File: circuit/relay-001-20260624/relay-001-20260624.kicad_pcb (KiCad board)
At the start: 2 copper layers, 169 x 126.3 mm, 15 parts, among them J1 Conn_01x03_Pin, J10 Conn_01x02_Pin, J11 Conn_01x02_Pin, J12 Conn_01x02_Pin, J13 Conn_01x02_Pin, J14 Conn_01x02_Pin, J15 Conn_01x02_Pin, J2 Conn_02x05_Odd_Even, J3 Conn_02x08_Odd_Even, J4 Conn_02x09_Odd_Even, J5 Conn_01x02_Pin, J6 Conn_01x02_Pin, J7 Conn_01x02_Pin, J8 Conn_01x02_Pin, J9 Conn_01x02_Pin

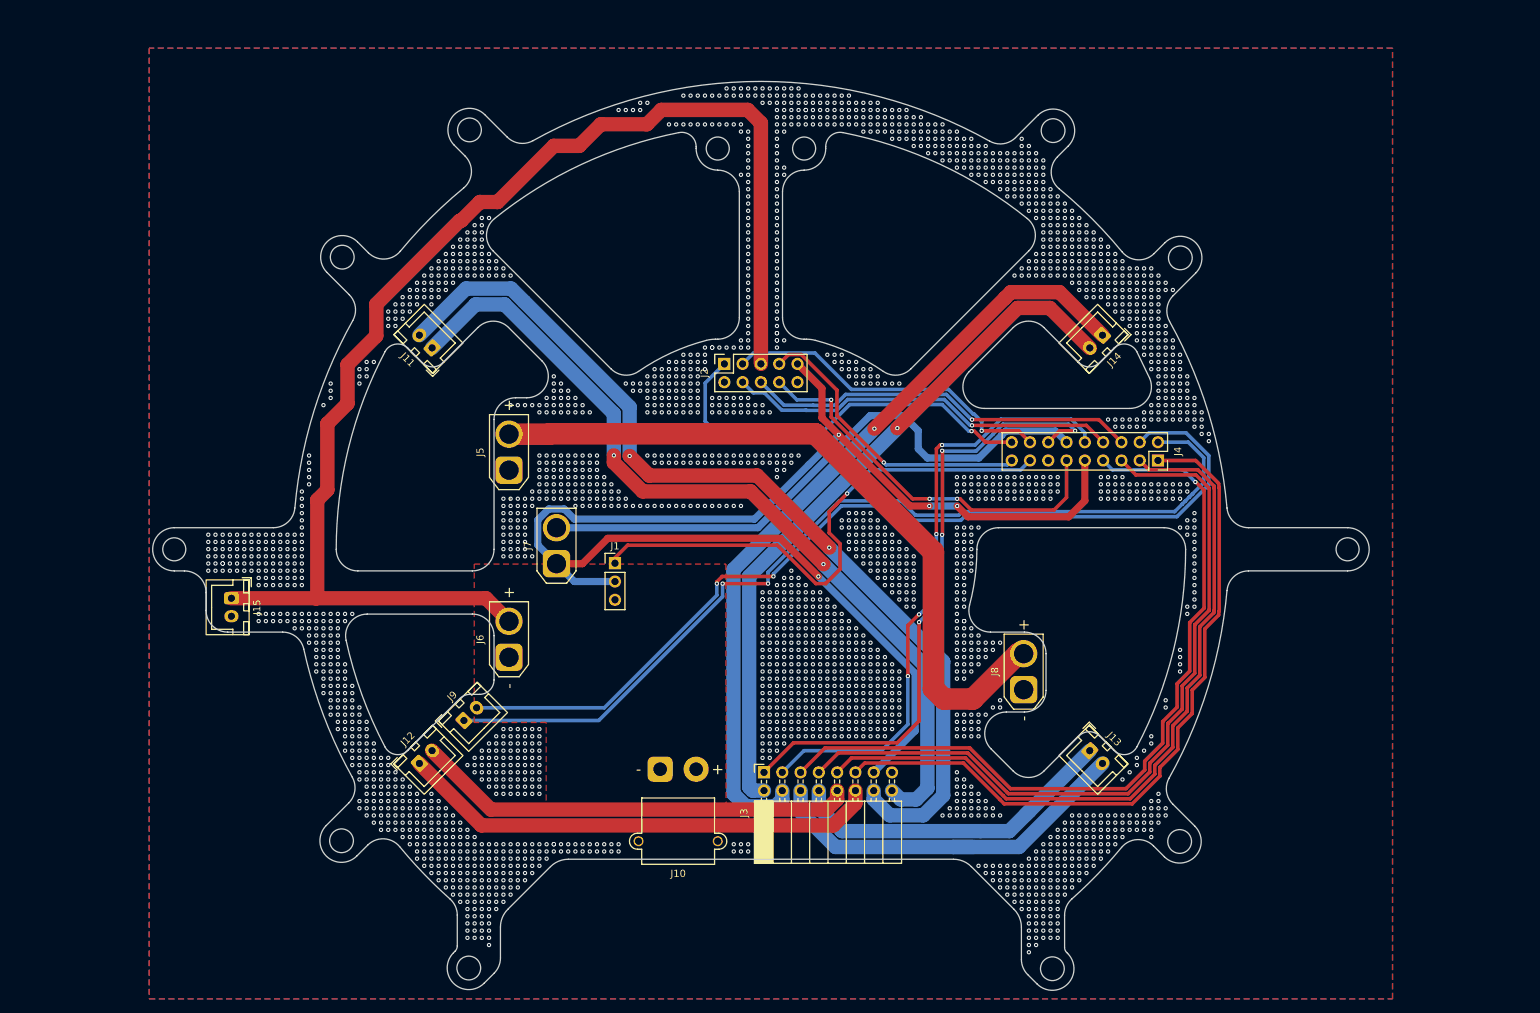
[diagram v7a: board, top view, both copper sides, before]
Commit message: Update 供給基板PCBデータと3Dファイル更新
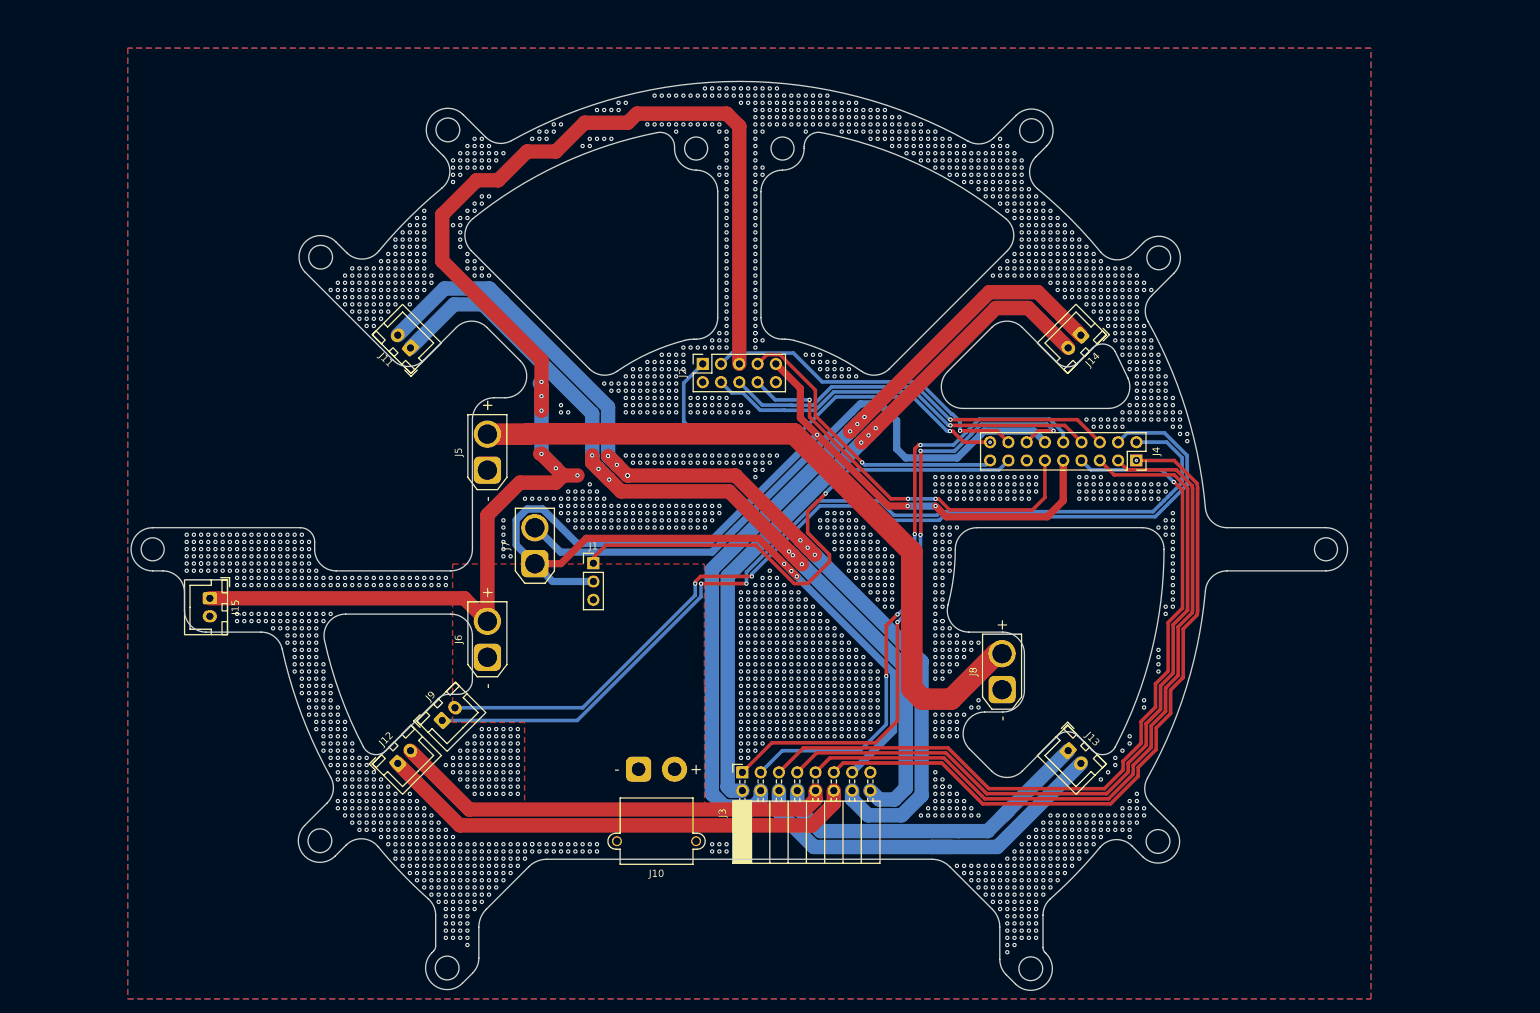
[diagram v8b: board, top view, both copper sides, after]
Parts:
- moved J1 3.00 mm to (108.5, 98.0)
- moved J10 3.00 mm to (114.8, 126.6)
- moved J11 3.00 mm to (83.1, 68.0)
- moved J12 3.00 mm to (81.3, 125.8)
- moved J13 3.00 mm to (174.5, 124.0)
- moved J14 3.00 mm to (176.2, 66.3)
- moved J15 3.00 mm to (55.2, 102.8)
- moved J2 3.00 mm to (123.7, 70.3)
- moved J3 3.00 mm to (129.2, 127.0)
- moved J4 3.00 mm to (183.9, 83.7)
- moved J5 3.00 mm to (93.8, 85.0)
- moved J6 3.00 mm to (93.8, 111.0)
- moved J7 3.00 mm to (100.4, 98.0)
- moved J8 3.00 mm to (165.3, 115.5)
- moved J9 3.00 mm to (87.5, 119.8)
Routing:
- net VCC: track 183.0 -> 202.3 mm, vias 0 -> 6
- net Motor_{OUT1-1}: track 119.0 -> 125.8 mm, vias 2 -> 6
- net +3.3V: track 197.0 -> 202.3 mm, vias 4 -> 6
- net +5V: track 83.4 -> 88.4 mm
- net Motor_{OUT1-2}: track 132.4 -> 137.0 mm, vias 2 -> 7
- net Motor_{OUT4-1}: track 110.0 -> 112.8 mm, vias 1 -> 3
- net Motor_{OUT4-2}: track 96.6 -> 99.4 mm, vias 1 -> 3
- net Dribbler_{Back}: track 75.3 -> 76.8 mm
- net EN_{Boost}: track 56.0 -> 56.9 mm
- net EN_{Dribbler-Front}: track 54.8 -> 55.7 mm
- net PH_{Dribbler-Front}: track 54.8 -> 55.7 mm
- net GND: vias 2549 -> 2634
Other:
- outline, holes or cut-outs redrawn
